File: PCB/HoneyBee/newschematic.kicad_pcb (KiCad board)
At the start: 4 copper layers, 50 x 50 mm, 42 parts, among them J1 S2B-PH-K-SLFSN, J2 10104110-0001LF, J3 01x05_MountingPin, M1 Motor_DC, M2 Motor_DC, M3 Motor_DC, M4 Motor_DC, M5 Motor_DC, M6 Motor_DC, Q1 IRLML2502TRPbF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

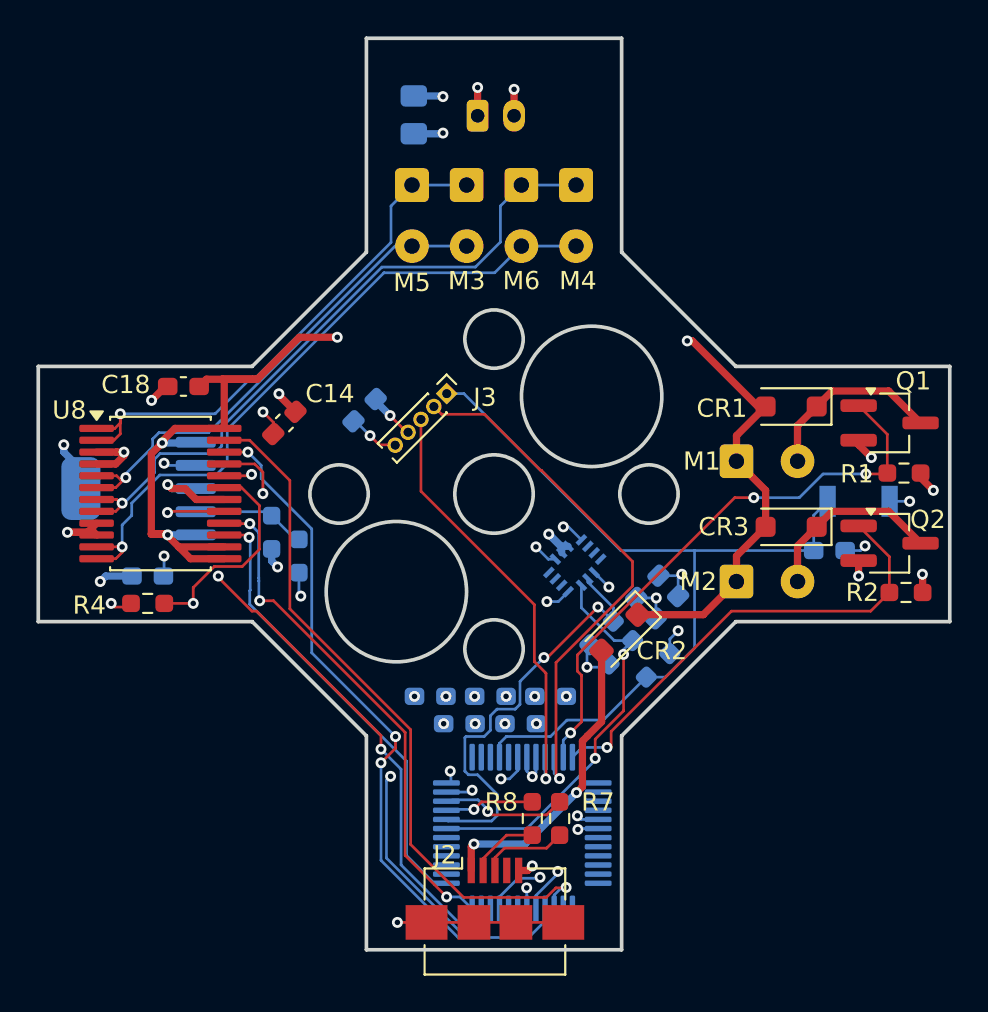
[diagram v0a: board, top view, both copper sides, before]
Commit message: Added power and signal LEDs, Added text
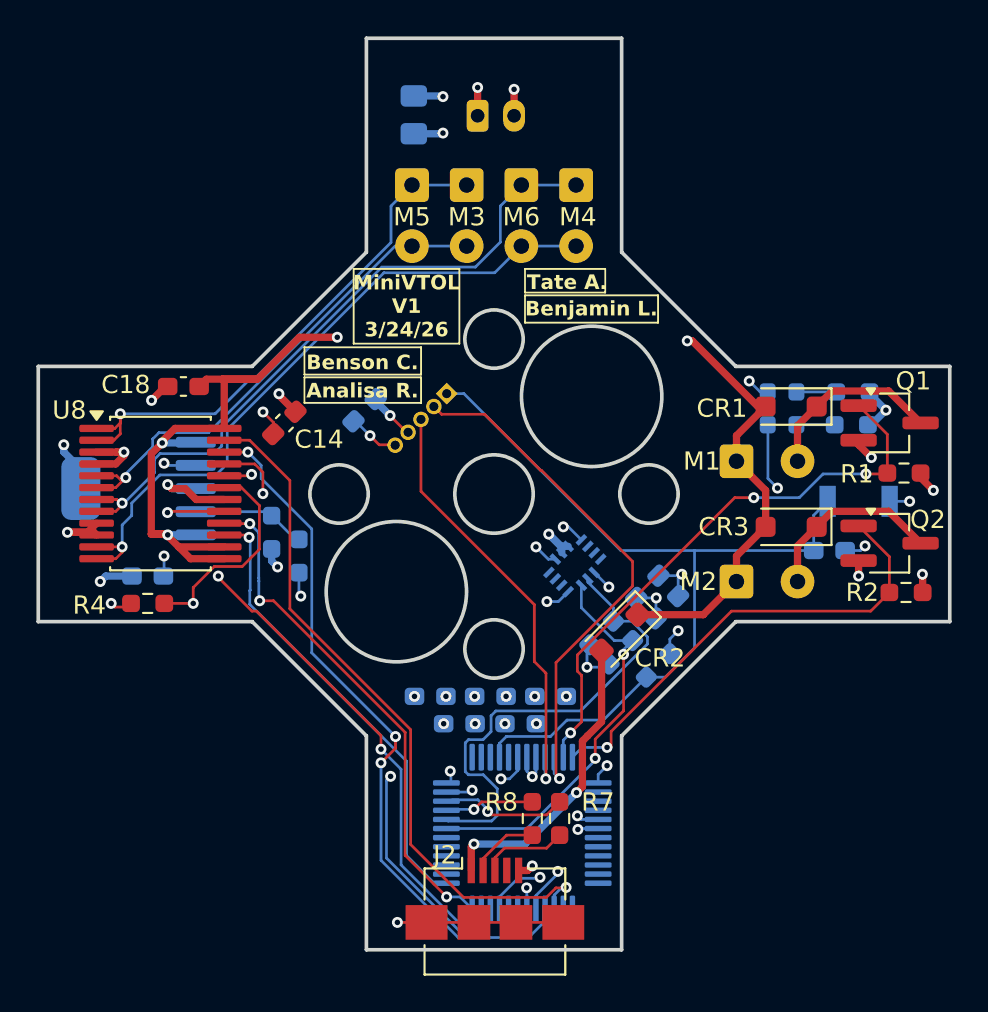
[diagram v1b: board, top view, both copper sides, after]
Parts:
- added D1: LED, LED_SMD:LED_0603_1608Metric, B.Cu at (115.8, 61.2)
- added D2: LED, LED_SMD:LED_0603_1608Metric, B.Cu at (115.8, 59.4)
- added R11: 330, Resistor_SMD:R_0603_1608Metric_Pad0.98x0.95mm_HandSolder, B.Cu at (119.6, 61.2)
- added R12: 330, Resistor_SMD:R_0603_1608Metric_Pad0.98x0.95mm_HandSolder, B.Cu at (119.7, 59.4)
- J3: moved to B.Cu
- turned J3 to 135 degrees
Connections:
- U1 pad 1: unconnected-(U1-PA00-Pad1) -> Net-(D1-A)
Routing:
- net Net-(D1-A): track 0.00 -> 26.6 mm, vias 0 -> 2
- net Net-(U1-PA23): track 23.8 -> 26.4 mm, vias 2 -> 0
- net GND: track 53.0 -> 55.4 mm, vias 31 -> 32
- net Net-(D2-K): track 0.00 -> 2.19 mm
- net Net-(D1-K): track 0.00 -> 2.10 mm
- net +3.3V: track 26.7 -> 28.0 mm, vias 22 -> 23
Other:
- board text added: "Analisa R."
- board text added: "Benjamin L."
- board text added: "Benson C."
- board text added: "MiniVTOL V1 3/24/26"
- board text added: "Tate A."
